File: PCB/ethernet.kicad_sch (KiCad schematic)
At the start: 34 parts, among them IC24 ENC28J60-I_SO, J5 JXD2-0Z10NL, T1 PT61017XPEL, Y1 25MHz

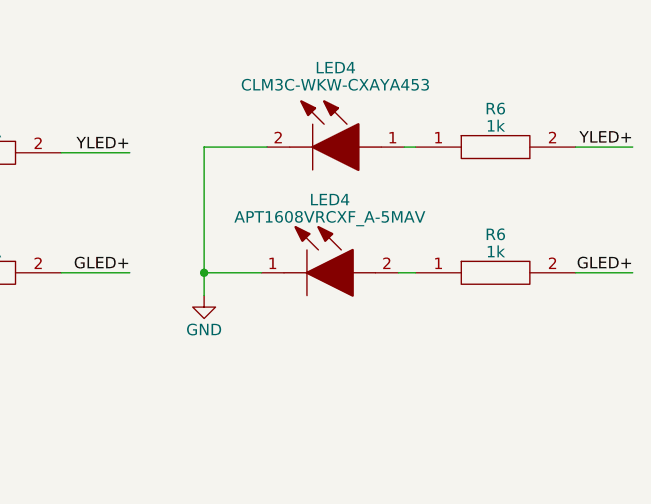
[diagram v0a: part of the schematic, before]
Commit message: switch polarity of cyan LED (closes #22)
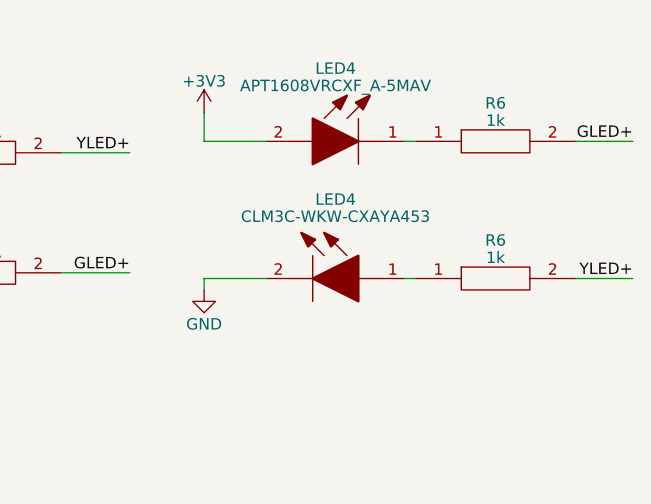
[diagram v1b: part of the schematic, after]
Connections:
- net +3V3: now also LED4.2
- net GND: no longer LED4.1
- net at R6.1: now also LED4.1; no longer LED4.2
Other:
- moved on the sheet: LED4, R6

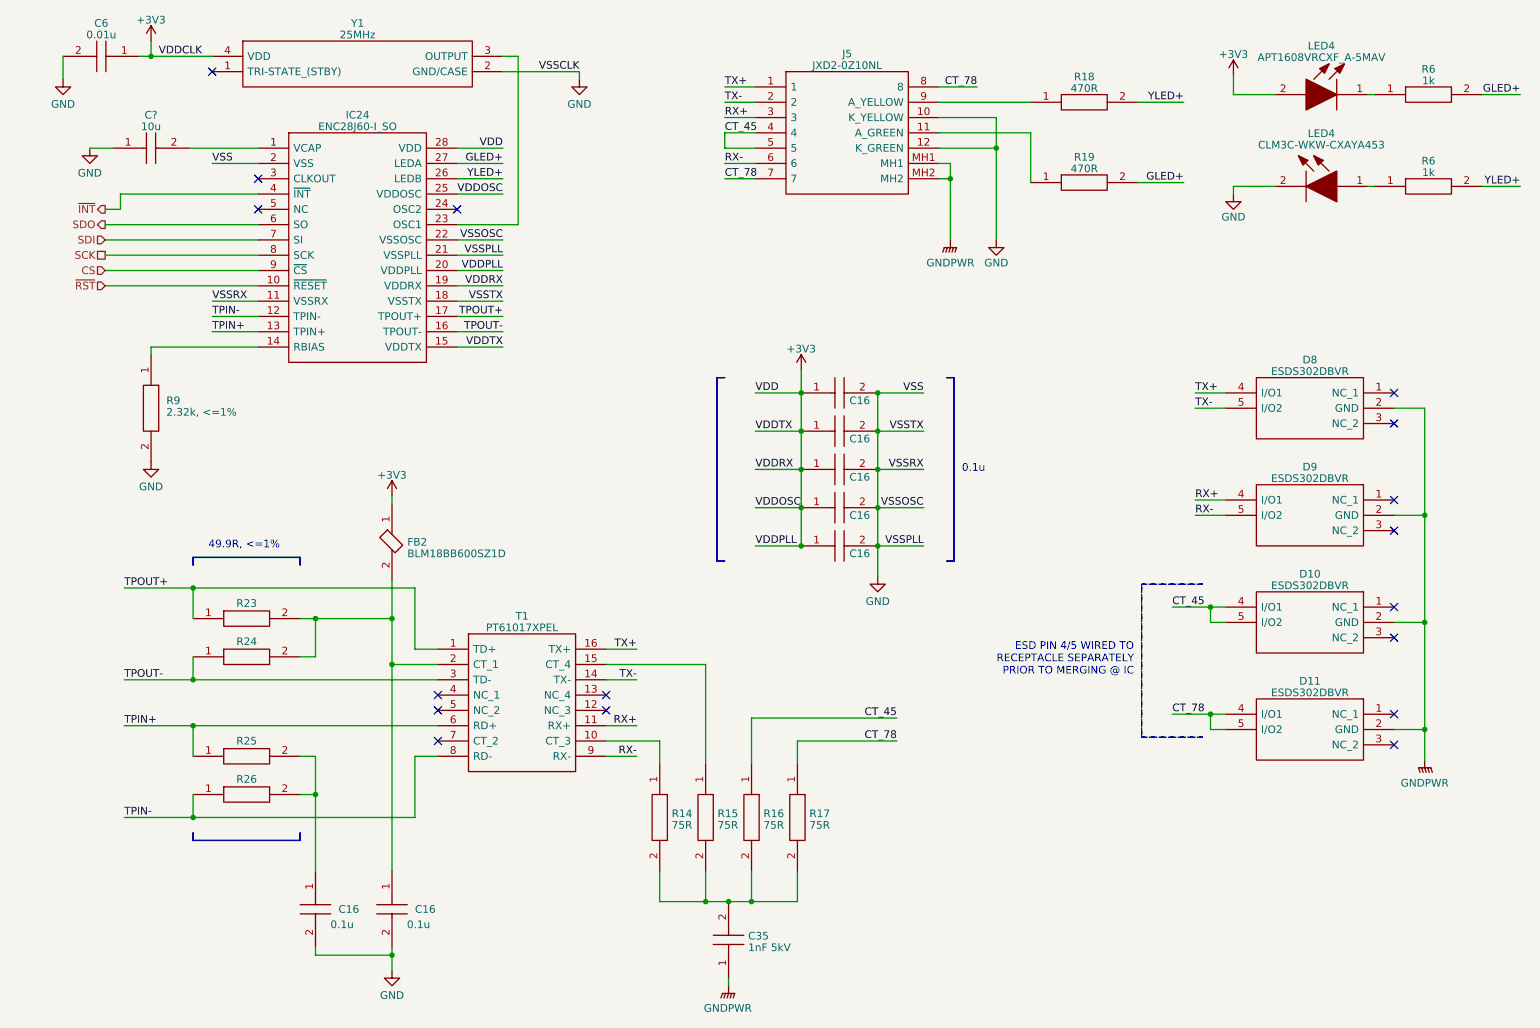
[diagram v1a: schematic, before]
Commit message: remove ESD ICs from ethernet port (closes #23)
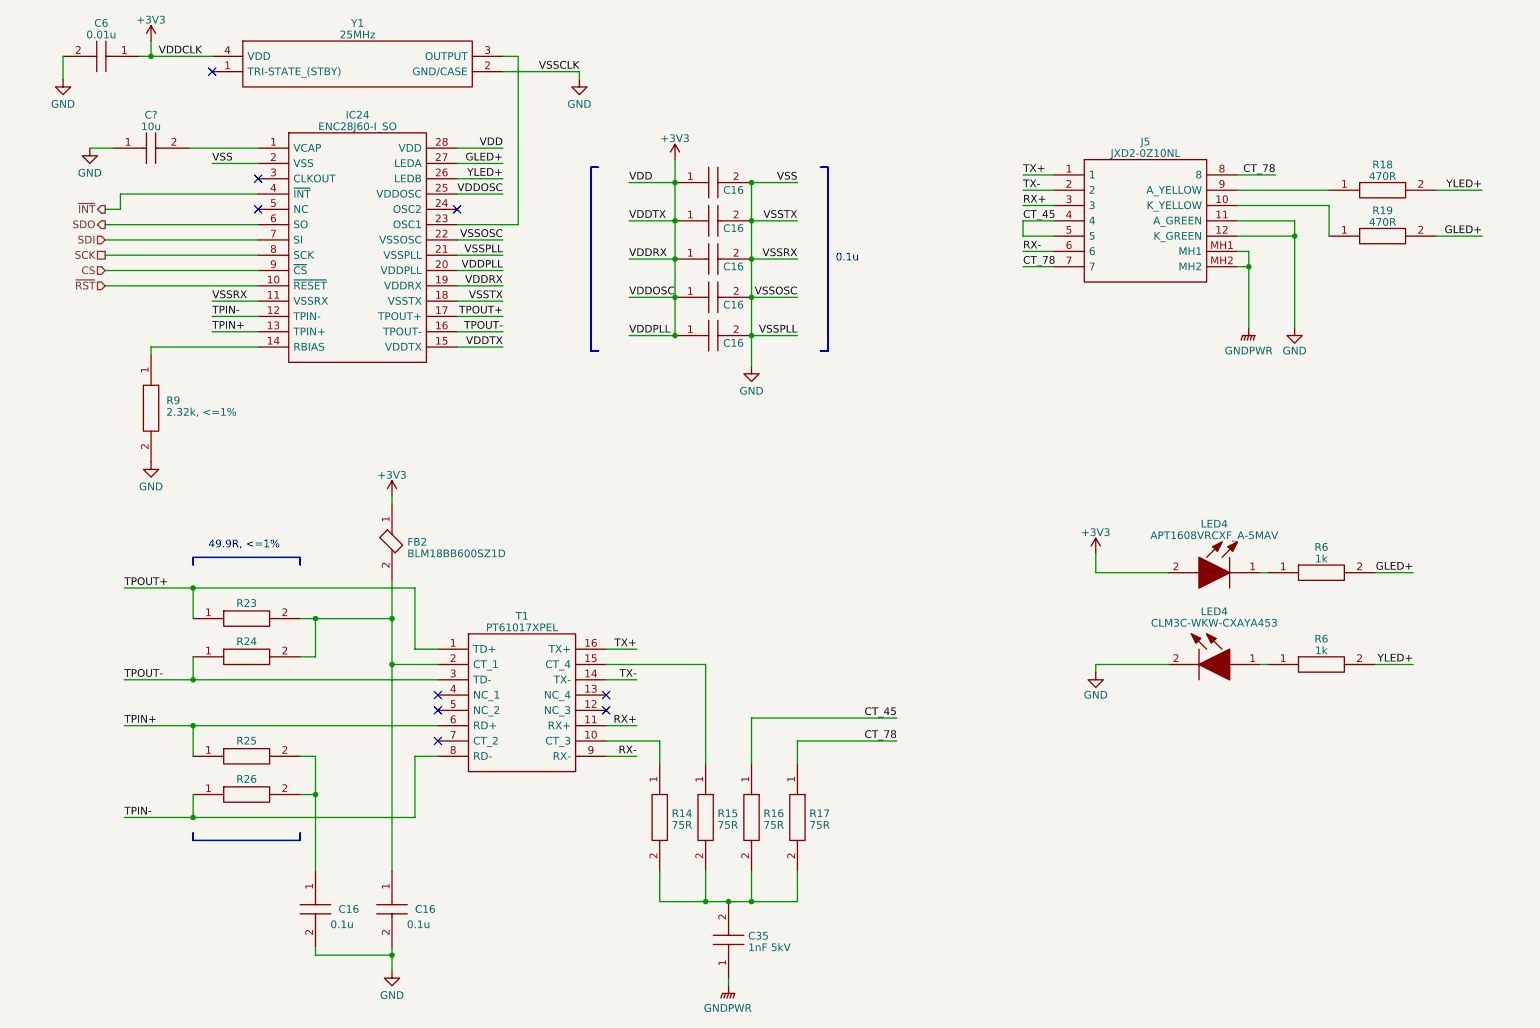
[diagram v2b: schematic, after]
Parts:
- removed D10, D11, D8, D9: ESDS302DBVR, SOT95P280X145-5N, symbol SamacSys_Parts:ESDS302DBVR
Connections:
- net GND: now also J5.11 (A_GREEN); no longer J5.10 (K_YELLOW)
- net at R19.1: now also J5.10 (K_YELLOW); no longer J5.11 (A_GREEN)
- no-connect marks 17 -> 9
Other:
- note removed: "ESD PIN 4/5 WIRED TO RECEPTACLE SEPARATELY PRIOR TO MERGING @ IC"
- moved on the sheet: C16, J5, LED4, R18, R19, R6

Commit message: switch to self-contained magnetics ethernet jack (closes #28)
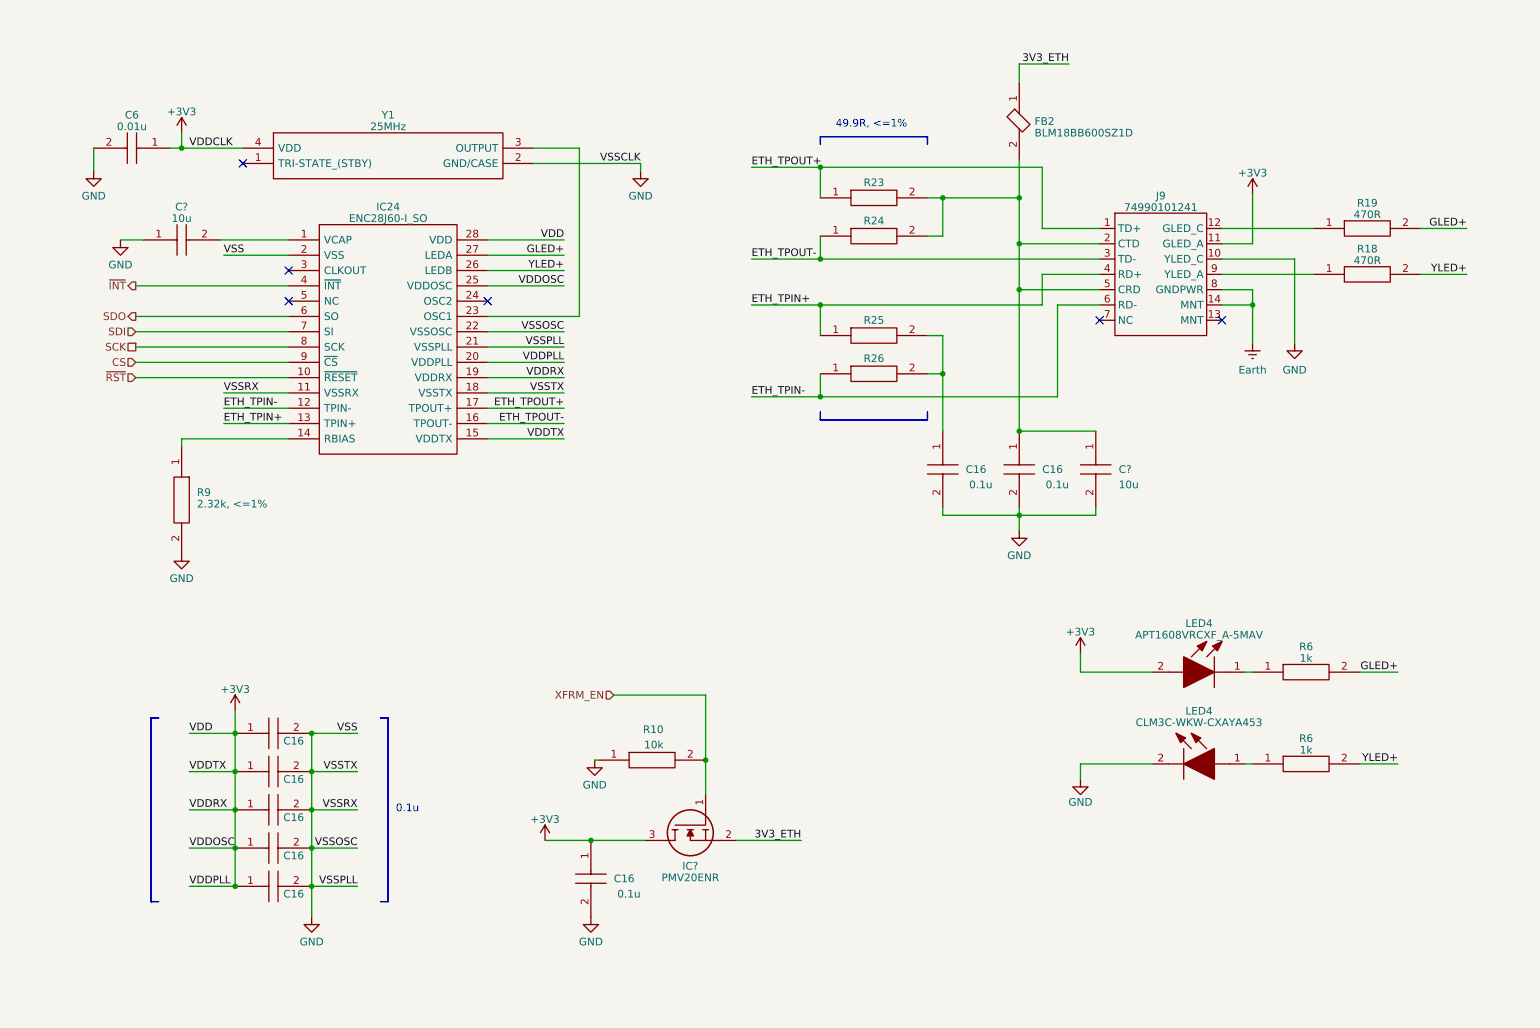
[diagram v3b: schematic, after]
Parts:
- removed C35: 1nF 5kV, CAPC5664X270N, symbol SamacSys_Parts:HV2225Y102KXMATHV
- removed J5: JXD2-0Z10NL, JXD20Z10NL, symbol SamacSys_Parts:JXD2-0Z10NL
- removed R14, R15, R16, R17: 75R, RESC1005X40N, symbol SamacSys_Parts:RK73H1ETTP75R0F
- removed T1: PT61017XPEL, SOIC127P930X570-16N, symbol SamacSys_Parts:PT61017XPEL
- added C16: 0.1u, SamacSys_Parts:CAPC0402X22N, symbol SamacSys_Parts:01016D104KAT2A
- added C?: 10u, SamacSys_Parts:CAPC2012X135N, symbol SamacSys_Parts:LMK212ABJ106KG8T
- added IC?: PMV20ENR, SamacSys_Parts:SOT95P230X110-3N, symbol SamacSys_Parts:CSD13380F3T
- added J9: 74990101241, Oro Footprints:74990101241, symbol Oro:74990101241
- added R10: 10k, SamacSys_Parts:RESC5025X65N, symbol SamacSys_Parts:RC2010JK-0710KL
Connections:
- net +3V3: now also C16.1, IC?.3, J9.11 (GLED_A); no longer FB2.1
- net GND: now also C16.2, C?.2, J9.10 (YLED_C), R10.1
- net at C16.1, FB2.2, R23.2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: now also C?.1, J9.2 (CTD), J9.5 (CRD)
- net at R19.1: now also J9.12 (GLED_C)
- net at R18.1: now also J9.9 (YLED_A)
- net TPIN+ renamed ETH_TPIN+
- net ETH_TPIN+: now also J9.4 (RD+)
- net TPIN- renamed ETH_TPIN-
- net ETH_TPIN-: now also J9.6 (RD-)
- net TPOUT+ renamed ETH_TPOUT+
- net ETH_TPOUT+: now also J9.1 (TD+)
- net TPOUT- renamed ETH_TPOUT-
- net ETH_TPOUT-: now also J9.3 (TD-)
- new net 3V3_ETH: FB2.1, IC?.2
- new net Earth: J9.14 (MNT), J9.8 (GNDPWR)
- new net XFRM_EN: IC?.1, R10.2
- no-connect marks 9 -> 6
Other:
- moved on the sheet: C16, C6, C?, FB2, IC24, LED4, R18, R19, R23, R24, R25, R26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

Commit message: re-annotate schematic
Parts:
- renumbered J9 to J6, LED4 to LED5, R19 to R17, R23 to R21, R24 to R22, R25 to R23, R26 to R24

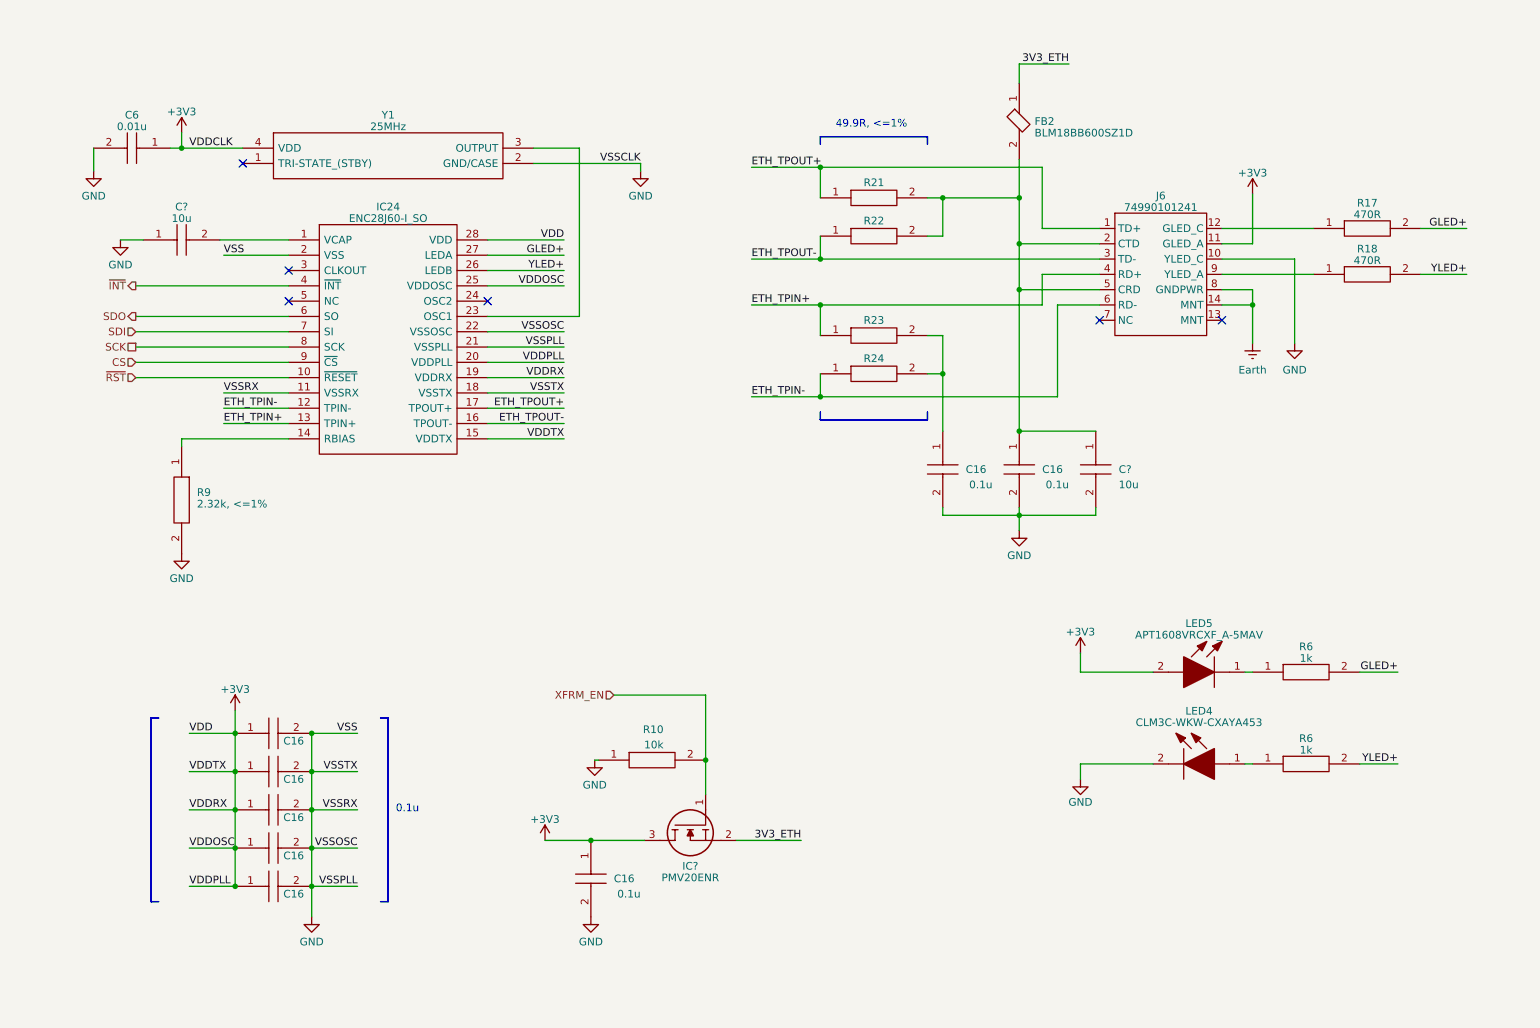
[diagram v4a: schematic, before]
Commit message: add pullup/down resistors and fix oro 6p lines with boot1/0
closes #24
closes #21
closes #15
closes #12
closes #6
closes #3
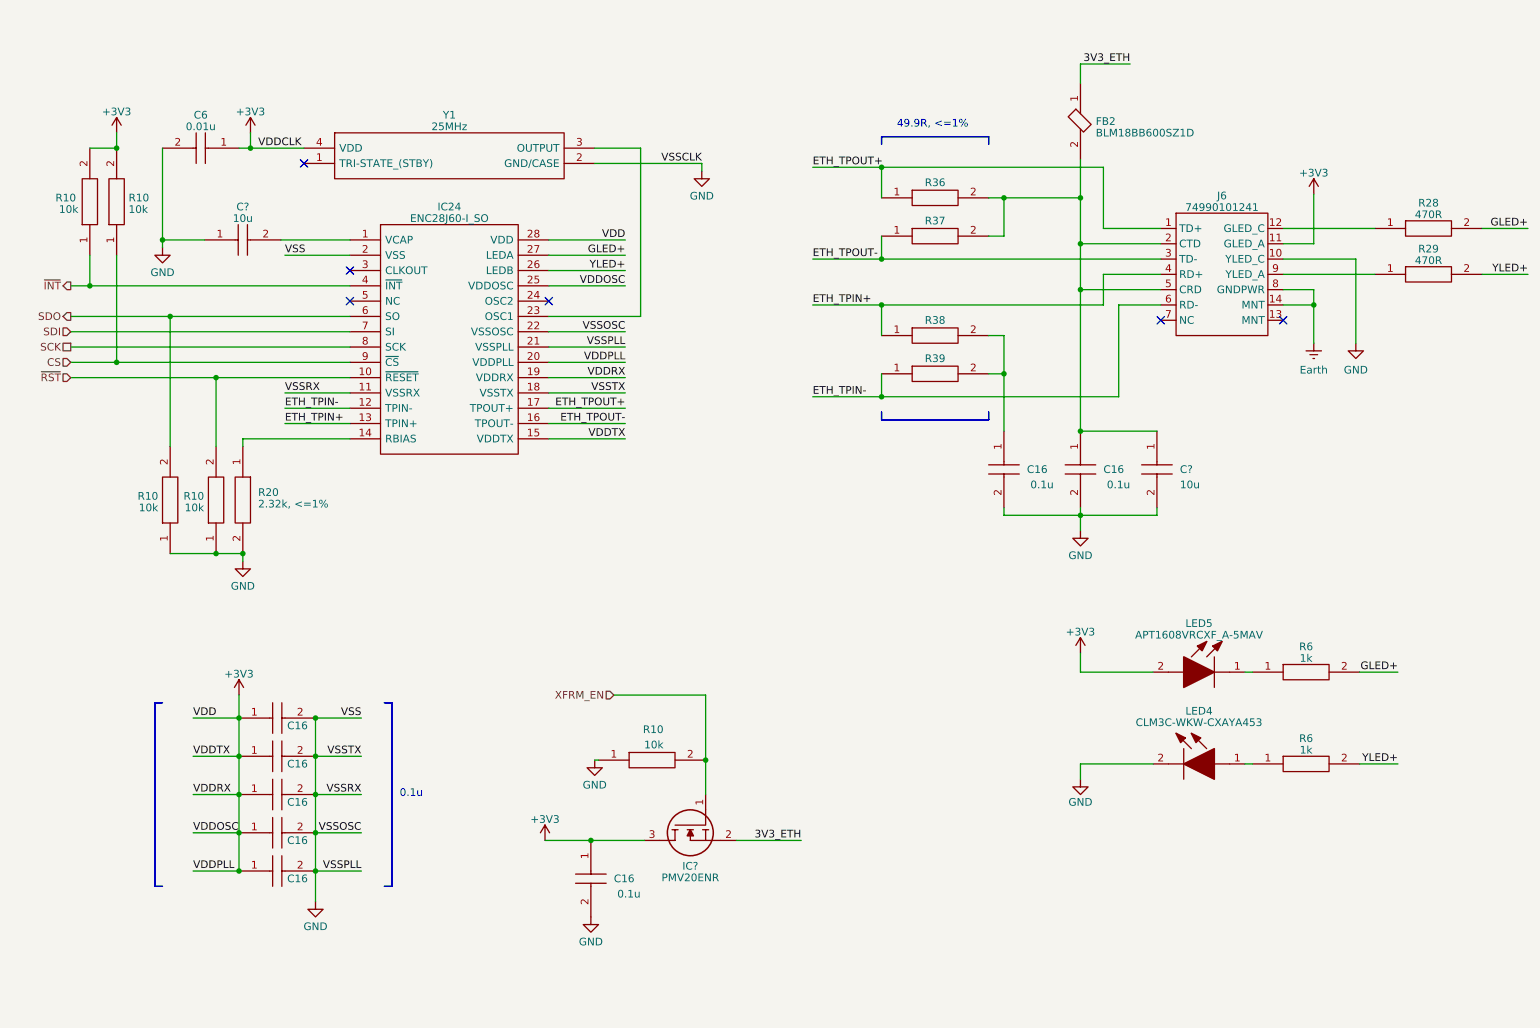
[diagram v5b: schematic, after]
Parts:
- added R10 (x4): 10k, SamacSys_Parts:RESC5025X65N, symbol SamacSys_Parts:RC2010JK-0710KL
- renumbered R9 to R20, R17 to R28, R18 to R29, R21 to R36, R22 to R37, R23 to R38, R24 to R39
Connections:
- net +3V3: now also R10.2, R10.2
- net CS: now also R10.1
- net GND: now also R10.1, R10.1
- net SDO: now also R10.2
- net ~{INT}: now also R10.1
- net ~{RST}: now also R10.2
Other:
- moved on the sheet: C16, C6, C?, FB2, IC24, J6, R20, R28, R29, R36, R37, R38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
